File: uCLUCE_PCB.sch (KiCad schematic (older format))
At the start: 19 parts, among them J1 Screw_Terminal_01x03, J2 GS2, P1 USB_A, P2 UART_TTL, U1 PIC16F1455-I/ST, U2 MCP2003B-E/SN, U3 fiducial

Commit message: gerber generation
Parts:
- removed P2: UART_TTL, Pin_Headers:Pin_Header_Straight_1x02_Pitch2.54mm, symbol CONN_01X02
- added P2: UART_TTL, Pin_Headers:Pin_Header_Straight_1x03_Pitch2.54mm, symbol CONN_01X03
- C1, C2, C3: 1st Disrtib Link (none) -> https://www.maritex.com.pl/elementy_pasywne/kondensatory/ko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
- C4, C5: footprint (none) -> Capacitors_SMD:C_0603; 1st Disrtib Link (none) -> https://www.maritex.com.pl/elementy_pasywne/kondensatory/ko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
- R1, R2, R3: 1st Disrtib Link (none) -> https://www.maritex.com.pl/elementy_pasywne/rezystory/rezys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
- U2: footprint Housings_SOIC:SO-8_5.3x6.2mm_Pitch1.27mm -> Housings_SOIC:SOIC-8_3.9x4.9mm_Pitch1.27mm
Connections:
- net GND: now also P2.3 (P3)
- net at R2.1, U1.6 (RC4), U2.1 (Rxd): now also P2.2 (P2)
- net at U1.5 (RC5), U2.4 (TXd): now also P2.1 (P1)
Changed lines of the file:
@@
 F 0 "U2" H 3050 2850 60  0000 C CNN
 F 1 "MCP2003B-E/SN" H 3150 2250 60  0000 C CNN
-F 2 "Housings_SOIC:SO-8_5.3x6.2mm_Pitch1.27mm" H 3000 2350 60  0001 C CNN
+F 2 "Housings_SOIC:SOIC-8_3.9x4.9mm_Pitch1.27mm" H 3000 2350 60  0001 C CNN
 F 3 "" H 3000 2350 60  0001 C CNN
 F 4 "https://octopart.com/mcp2003b-e%2Fsn-microchip-67312985" H 3250 2550 60  0001 C CNN "1st Disrtib Link"
@@
 F 2 "Capacitors_SMD:C_0603" H 6050 2300 50  0001 C CNN
 F 3 "" H 6050 2300 50  0001 C CNN
+F 4 "https://www.maritex.com.pl/elementy_pasywne/kondensatory/kondensatory_ceramiczne/smd_0603/dielektryk_x7r_lub_x5r/cmc0603-470n-kx25-s.html" H 6050 2300 60  0001 C CNN "1st Disrtib Link"
 	1    6050 2300
 	0    1    1    0
 $EndComp
 $Comp
-L GND #PWR16
+L GND #PWR01
 U 1 1 59E21FB8
 P 7350 2150
-F 0 "#PWR16" H 7350 1900 50  0001 C CNN
+F 0 "#PWR01" H 7350 1900 50  0001 C CNN
 F 1 "GND" H 7350 2000 50  0000 C CNN
 F 2 "" H 7350 2150 50  0001 C CNN
@@
 $EndComp
 $Comp
-L +5V #PWR15
+L +5V #PWR02
 U 1 1 59E220C9
 P 6950 2900
-F 0 "#PWR15" H 6950 2750 50  0001 C CNN
+F 0 "#PWR02" H 6950 2750 50  0001 C CNN
 F 1 "+5V" H 6950 3040 50  0000 C CNN
 F 2 "" H 6950 2900 50  0001 C CNN
@@
 $EndComp
 $Comp
-L +5V #PWR11
+L +5V #PWR03
 U 1 1 59E2213F
 P 4050 2000
-F 0 "#PWR11" H 4050 1850 50  0001 C CNN
+F 0 "#PWR03" H 4050 1850 50  0001 C CNN
 F 1 "+5V" H 4050 2140 50  0000 C CNN
 F 2 "" H 4050 2000 50  0001 C CNN
@@
 $EndComp
 $Comp
-L +BATT #PWR1
+L +BATT #PWR04
 U 1 1 59E22154
 P 2000 2200
-F 0 "#PWR1" H 2000 2050 50  0001 C CNN
+F 0 "#PWR04" H 2000 2050 50  0001 C CNN
 F 1 "+BATT" V 1950 2400 50  0000 C CNN
 F 2 "" H 2000 2200 50  0001 C CNN
@@
 $EndComp
 $Comp
-L GND #PWR2
+L GND #PWR05
 U 1 1 59E22180
 P 2400 2200
-F 0 "#PWR2" H 2400 1950 50  0001 C CNN
+F 0 "#PWR05" H 2400 1950 50  0001 C CNN
 F 1 "GND" V 2300 2100 50  0000 C CNN
 F 2 "" H 2400 2200 50  0001 C CNN
@@
 $EndComp
 $Comp
-L GND #PWR14
+L GND #PWR06
 U 1 1 59E230A7
 P 6950 2800
-F 0 "#PWR14" H 6950 2550 50  0001 C CNN
+F 0 "#PWR06" H 6950 2550 50  0001 C CNN
 F 1 "GND" V 6900 2600 50  0001 C CNN
 F 2 "" H 6950 2800 50  0001 C CNN
@@
 MCLR
 $Comp
-L +5V #PWR13
+L +5V #PWR07
 U 1 1 59E237FB
 P 6550 2300
-F 0 "#PWR13" H 6550 2150 50  0001 C CNN
+F 0 "#PWR07" H 6550 2150 50  0001 C CNN
 F 1 "+5V" H 6550 2440 50  0000 C CNN
 F 2 "" H 6550 2300 50  0001 C CNN
@@
 F 2 "Capacitors_SMD:C_0603" H 3450 1850 50  0001 C CNN
 F 3 "" H 3450 1850 50  0001 C CNN
+F 4 "https://www.maritex.com.pl/elementy_pasywne/kondensatory/kondensatory_ceramiczne/smd_0603/dielektryk_x7r_lub_x5r/cmc0603-470n-kx25-s.html" H 3450 1850 60  0001 C CNN "1st Disrtib Link"
 	1    3450 1850
 	-1   0    0    1
 $EndComp
 $Comp
-L +5V #PWR7
+L +5V #PWR08
 U 1 1 59E2335A
 P 3450 1750
-F 0 "#PWR7" H 3450 1600 50  0001 C CNN
+F 0 "#PWR08" H 3450 1600 50  0001 C CNN
 F 1 "+5V" H 3450 1890 50  0000 C CNN
 F 2 "" H 3450 1750 50  0001 C CNN
@@
 $EndComp
 $Comp
-L GND #PWR8
+L GND #PWR09
 U 1 1 59E2337A
 P 3450 1950
-F 0 "#PWR8" H 3450 1700 50  0001 C CNN
+F 0 "#PWR09" H 3450 1700 50  0001 C CNN
 F 1 "GND" H 3450 1800 50  0001 C CNN
 F 2 "" H 3450 1950 50  0001 C CNN
@@
 $EndComp
 $Comp
-L +5V #PWR9
+L +5V #PWR010
 U 1 1 59E233BF
 P 3750 1750
-F 0 "#PWR9" H 3750 1600 50  0001 C CNN
+F 0 "#PWR010" H 3750 1600 50  0001 C CNN
 F 1 "+5V" H 3750 1890 50  0000 C CNN
 F 2 "" H 3750 1750 50  0001 C CNN
@@
 $EndComp
 $Comp
-L GND #PWR10
+L GND #PWR011
 U 1 1 59E23423
 P 3750 1950
-F 0 "#PWR10" H 3750 1700 50  0001 C CNN
+F 0 "#PWR011" H 3750 1700 50  0001 C CNN
 F 1 "GND" H 3750 1800 50  0001 C CNN
 F 2 "" H 3750 1950 50  0001 C CNN
@@
 F 2 "Resistors_SMD:R_0603" H 2650 1450 50  0001 C CNN
 F 3 "" H 2650 1450 50  0001 C CNN
+F 4 "https://www.maritex.com.pl/elementy_pasywne/rezystory/rezystory_smd/rezystory_smd_0603/rezystory_smd_w_rozmiarze_0603_w_tolerancji_5/rmc0603-1k0-s.html" H 2650 1450 60  0001 C CNN "1st Disrtib Link"
 	1    2650 1450
 	1    0    0    -1
 $EndComp
 $Comp
-L +BATT #PWR3
+L +BATT #PWR012
 U 1 1 59E23A89
 P 2650 1050
-F 0 "#PWR3" H 2650 900 50  0001 C CNN
+F 0 "#PWR012" H 2650 900 50  0001 C CNN
 F 1 "+BATT" H 2650 1190 50  0000 C CNN
 F 2 "" H 2650 1050 50  0001 C CNN
@@
 F 2 "Capacitors_SMD:C_0603" H 3750 1850 50  0001 C CNN
 F 3 "" H 3750 1850 50  0001 C CNN
+F 4 "https://www.maritex.com.pl/elementy_pasywne/kondensatory/kondensatory_ceramiczne/smd_0603/dielektryk_x7r_lub_x5r/cmc0603-100n-kx16-s.html" H 3750 1850 60  0001 C CNN "1st Disrtib Link"
 	1    3750 1850
 	-1   0    0    1
@@
 F 2 "Resistors_SMD:R_0603" H 3950 2600 50  0001 C CNN
 F 3 "" H 3950 2600 50  0001 C CNN
+F 4 "https://www.maritex.com.pl/elementy_pasywne/rezystory/rezystory_smd/rezystory_smd_0603/rezystory_smd_0603_w_tolerancji_1/rmc0603-4k7-1-y.html" H 3950 2600 60  0001 C CNN "1st Disrtib Link"
 	1    3950 2600
 	1    0    0    -1
 $EndComp
 $Comp
-L GND #PWR5
+L GND #PWR013
 U 1 1 59E51428
 P 2800 2150
-F 0 "#PWR5" H 2800 1900 50  0001 C CNN
+F 0 "#PWR013" H 2800 1900 50  0001 C CNN
 F 1 "GND" H 2800 2000 50  0001 C CNN
 F 2 "" H 2800 2150 50  0001 C CNN
@@
 $EndComp
 $Comp
-L +5V #PWR12
+L +5V #PWR014
 U 1 1 59E50C40
 P 4150 2950
-F 0 "#PWR12" H 4150 2800 50  0001 C CNN
+F 0 "#PWR014" H 4150 2800 50  0001 C CNN
 F 1 "+5V" H 4150 3090 50  0000 C CNN
 F 2 "" H 4150 2950 50  0001 C CNN
@@
 F 0 "C5" H 2910 2970 50  0000 L CNN
 F 1 "1u" H 2910 2820 50  0000 L CNN
-F 2 "" H 2900 2900 50  0000 C CNN
+F 2 "Capacitors_SMD:C_0603" H 2900 2900 50  0001 C CNN
 F 3 "" H 2900 2900 50  0000 C CNN
+F 4 "https://www.maritex.com.pl/elementy_pasywne/kondensatory/kondensatory_ceramiczne/smd_0603/dielektryk_x7r_lub_x5r/cmc0603-1000n-kx16-s.html" H 2900 2900 60  0001 C CNN "1st Disrtib Link"
 	1    2900 2900
 	1    0    0    -1
@@
 F 0 "C4" H 2810 2120 50  0000 L CNN
 F 1 "220p" H 2810 1970 50  0000 L CNN
-F 2 "" H 2800 2050 50  0000 C CNN
+F 2 "Capacitors_SMD:C_0603" H 2800 2050 50  0001 C CNN
 F 3 "" H 2800 2050 50  0000 C CNN
+F 4 "https://www.maritex.com.pl/elementy_pasywne/kondensatory/kondensatory_ceramiczne/smd_0603/dielektryk_x7r_lub_x5r/cmc0603-680p-kx16-f.html" H 2800 2050 60  0001 C CNN "1st Disrtib Link"
 	1    2800 2050
 	1    0    0    -1
@@
 $EndComp
 $Comp
-L GND #PWR4
+L GND #PWR015
 U 1 1 59E668FA
 P 2700 3000
-F 0 "#PWR4" H 2700 2750 50  0001 C CNN
+F 0 "#PWR015" H 2700 2750 50  0001 C CNN
 F 1 "GND" H 2700 2850 50  0000 C CNN
 F 2 "" H 2700 3000 50  0001 C CNN
@@
 F 2 "Resistors_SMD:R_0603" H 2550 2600 50  0001 C CNN
 F 3 "" H 2550 2600 50  0001 C CNN
+F 4 "https://www.maritex.com.pl/elementy_pasywne/rezystory/rezystory_smd/rezystory_smd_0603/rezystory_smd_w_rozmiarze_0603_w_tolerancji_5/rmc0603-51r-y.html" H 2550 2600 60  0001 C CNN "1st Disrtib Link"
 	1    2550 2600
 	0    1    1    0
@@
 Connection ~ 2700 2800
 $Comp
-L GND #PWR6
+L GND #PWR016
 U 1 1 59E67A70
 P 2900 3000
-F 0 "#PWR6" H 2900 2750 50  0001 C CNN
+F 0 "#PWR016" H 2900 2750 50  0001 C CNN
 F 1 "GND" H 2900 2850 50  0000 C CNN
 F 2 "" H 2900 3000 50  0001 C CNN
@@
 	1900 2600 2050 2600
 Connection ~ 2000 2600
-$Comp
-L CONN_01X02 P2
-U 1 1 59E765D9
-P 3800 3400
-F 0 "P2" H 3800 3550 50  0000 C CNN
-F 1 "UART_TTL" V 3900 3400 50  0000 C CNN
-F 2 "Pin_Headers:Pin_Header_Straight_1x02_Pitch2.54mm" H 3800 3400 50  0001 C CNN
-F 3 "" H 3800 3400 50  0000 C CNN
-	1    3800 3400
-	0    1    1    0
-$EndComp
 Wire Wire Line
 	3750 3200 3750 2700
@@
 	1    0    0    -1
 $EndComp
+$Comp
+L CONN_01X03 P2
+U 1 1 59E7CE46
+P 3750 3400
+F 0 "P2" H 3750 3600 50  0000 C CNN
+F 1 "UART_TTL" V 3850 3400 50  0000 C CNN
+F 2 "Pin_Headers:Pin_Header_Straight_1x03_Pitch2.54mm" H 3750 3400 50  0001 C CNN
+F 3 "" H 3750 3400 50  0000 C CNN
+	1    3750 3400
+	0    1    1    0
+$EndComp
+$Comp
+L GND #PWR?
+U 1 1 59E7D0F4
+P 3650 3200
+F 0 "#PWR?" H 3650 2950 50  0001 C CNN
+F 1 "GND" H 3650 3050 50  0000 C CNN
+F 2 "" H 3650 3200 50  0001 C CNN
+F 3 "" H 3650 3200 50  0001 C CNN
+	1    3650 3200
+	0    1    1    0
+$EndComp
 $EndSCHEMATC

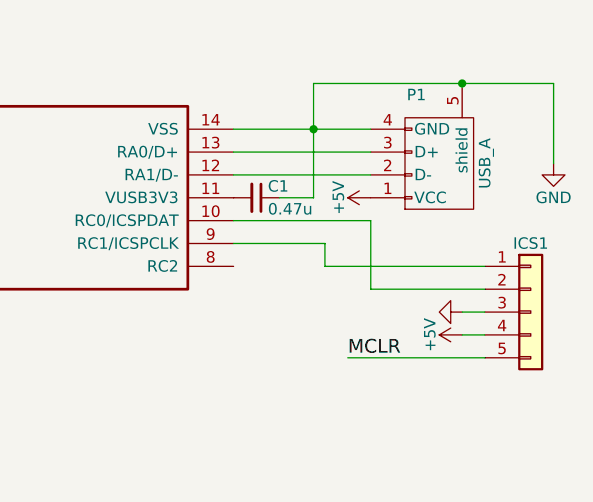
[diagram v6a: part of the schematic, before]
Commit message: Fixed USB Layout
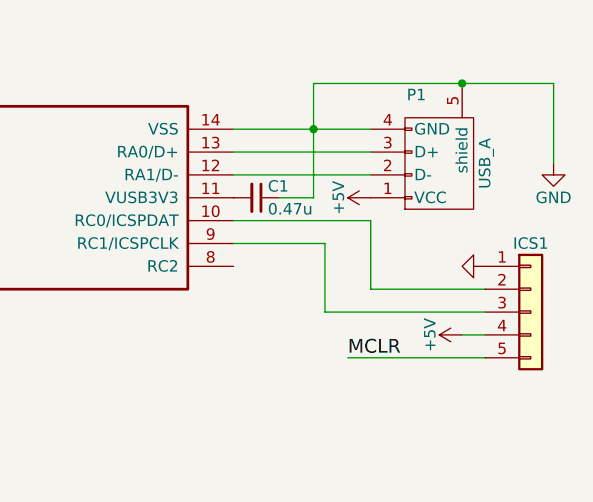
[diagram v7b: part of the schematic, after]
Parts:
- P1: footprint uCLUCE_PCB:USB_A_DS1097 -> uCLUCE_PCB:USB_A_DS1097R
- U3: footprint Fiducials:Fiducial_1mm_Dia_2.54mm_Outer_CopperBottom -> uCLUCE_PCB:FICUCIAL_MIN
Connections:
- net GND: now also ICS1.1 (Pin_1); no longer ICS1.3 (Pin_3)
- net at U1.9 (RC1/ICSPCLK): now also ICS1.3 (Pin_3); no longer ICS1.1 (Pin_1)
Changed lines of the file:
@@
 F 0 "P1" V 7100 2000 50  0000 C CNN
 F 1 "USB_A" H 6800 2300 50  0000 C CNN
-F 2 "uCLUCE_PCB:USB_A_DS1097" V 6800 2000 50  0001 C CNN
+F 2 "uCLUCE_PCB:USB_A_DS1097R" V 6800 2000 50  0001 C CNN
 F 3 "" V 6800 2000 50  0000 C CNN
 F 4 "https://www.maritex.com.pl/zlacza/zlacza_usb_hdmi_ieee/zlacza_i_kable_usb/wtyk_usb_1xa4_katowy/usbp1arw-cv.html" H 6850 2100 60  0001 C CNN "1st Disrtib Link"
@@
 L GND #PWR06
 U 1 1 59E230A7
-P 6950 2800
-F 0 "#PWR06" H 6950 2550 50  0001 C CNN
-F 1 "GND" V 6900 2600 50  0001 C CNN
-F 2 "" H 6950 2800 50  0001 C CNN
-F 3 "" H 6950 2800 50  0001 C CNN
-	1    6950 2800
+P 7050 2600
+F 0 "#PWR06" H 7050 2350 50  0001 C CNN
+F 1 "GND" V 7000 2400 50  0001 C CNN
+F 2 "" H 7050 2600 50  0001 C CNN
+F 3 "" H 7050 2600 50  0001 C CNN
+	1    7050 2600
 	0    1    1    0
 $EndComp
@@
 	7050 2900 6950 2900
 Wire Wire Line
-	7050 2800 6950 2800
-Wire Wire Line
-	6550 2700 7050 2700
-Wire Wire Line
-	6350 2600 7050 2600
-Wire Wire Line
-	6550 2700 6550 2400
-Wire Wire Line
 	6550 2400 5950 2400
 Wire Wire Line
-	6350 2600 6350 2500
+	6350 2500 6350 2800
 Wire Wire Line
 	6350 2500 5950 2500
@@
 F 0 "U3" H 6500 1400 60  0001 C CNN
 F 1 "fiducial" H 6900 1350 60  0000 C CNN
-F 2 "Fiducials:Fiducial_1mm_Dia_2.54mm_Outer_CopperBottom" H 6700 1150 60  0001 C CNN
+F 2 "uCLUCE_PCB:FICUCIAL_MIN" H 6700 1150 60  0001 C CNN
 F 3 "" H 6700 1150 60  0001 C CNN
 	1    6700 1150
@@
 $EndComp
 $Comp
-L GND #PWR?
+L GND #PWR017
 U 1 1 59E7D0F4
 P 3650 3200
-F 0 "#PWR?" H 3650 2950 50  0001 C CNN
+F 0 "#PWR017" H 3650 2950 50  0001 C CNN
 F 1 "GND" H 3650 3050 50  0000 C CNN
 F 2 "" H 3650 3200 50  0001 C CNN
@@
 	0    1    1    0
 $EndComp
+Wire Wire Line
+	6350 2800 7050 2800
+Wire Wire Line
+	6550 2700 6550 2400
+Wire Wire Line
+	6550 2700 7050 2700
 $EndSCHEMATC

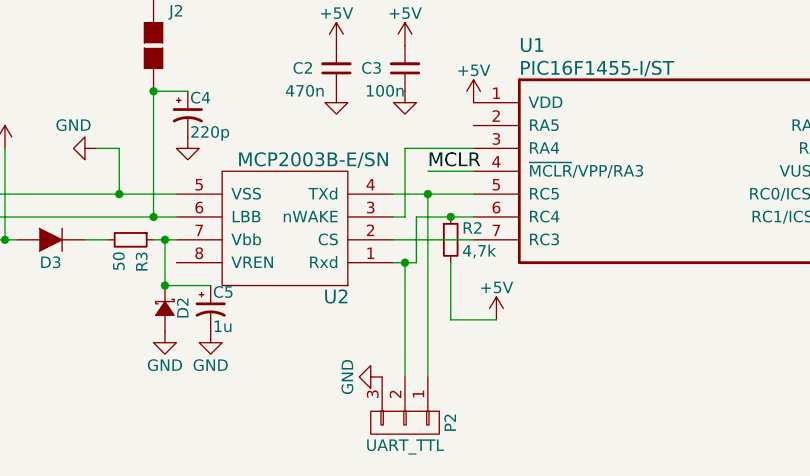
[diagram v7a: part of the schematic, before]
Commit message: Flip LIN RX/TX
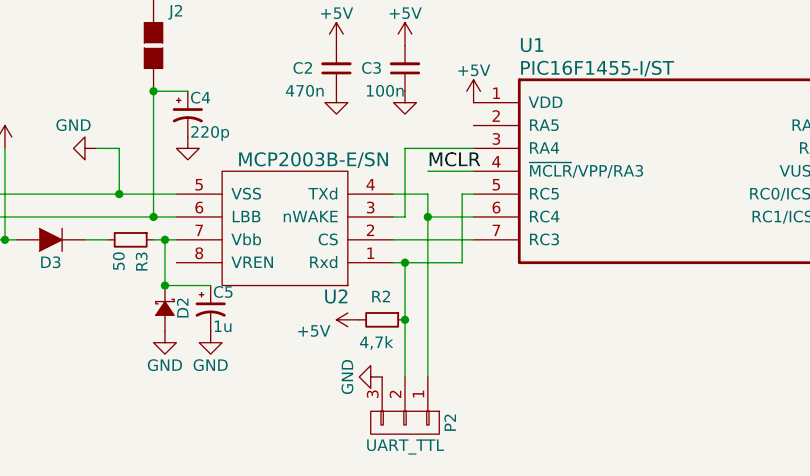
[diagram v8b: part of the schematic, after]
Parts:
- P1: footprint uCLUCE_PCB:USB_A_DS1097R -> uCLUCE_PCB:USB_A_DS1097
- U3: footprint uCLUCE_PCB:FICUCIAL_MIN -> Fiducials:Fiducial_1mm_Dia_2.54mm_Outer_CopperBottom
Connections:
- net at P2.2 (P2), R2.1, U2.1 (Rxd): now also U1.5 (RC5); no longer U1.6 (RC4)
- net at P2.1 (P1), U2.4 (TXd): now also U1.6 (RC4); no longer U1.5 (RC5)
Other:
- moved on the sheet: R2
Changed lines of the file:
@@
 F 0 "P1" V 7100 2000 50  0000 C CNN
 F 1 "USB_A" H 6800 2300 50  0000 C CNN
-F 2 "uCLUCE_PCB:USB_A_DS1097R" V 6800 2000 50  0001 C CNN
+F 2 "uCLUCE_PCB:USB_A_DS1097" V 6800 2000 50  0001 C CNN
 F 3 "" V 6800 2000 50  0000 C CNN
 F 4 "https://www.maritex.com.pl/zlacza/zlacza_usb_hdmi_ieee/zlacza_i_kable_usb/wtyk_usb_1xa4_katowy/usbp1arw-cv.html" H 6850 2100 60  0001 C CNN "1st Disrtib Link"
@@
 L R_Small R2
 U 1 1 59E50B0E
-P 3950 2600
-F 0 "R2" H 4000 2650 50  0000 L CNN
-F 1 "4,7k" H 4000 2550 50  0000 L CNN
-F 2 "Resistors_SMD:R_0603" H 3950 2600 50  0001 C CNN
-F 3 "" H 3950 2600 50  0001 C CNN
-F 4 "https://www.maritex.com.pl/elementy_pasywne/rezystory/rezystory_smd/rezystory_smd_0603/rezystory_smd_0603_w_tolerancji_1/rmc0603-4k7-1-y.html" H 3950 2600 60  0001 C CNN "1st Disrtib Link"
-	1    3950 2600
-	1    0    0    -1
+P 3650 2950
+F 0 "R2" V 3550 2900 50  0000 L CNN
+F 1 "4,7k" V 3750 2850 50  0000 L CNN
+F 2 "Resistors_SMD:R_0603" H 3650 2950 50  0001 C CNN
+F 3 "" H 3650 2950 50  0001 C CNN
+F 4 "https://www.maritex.com.pl/elementy_pasywne/rezystory/rezystory_smd/rezystory_smd_0603/rezystory_smd_0603_w_tolerancji_1/rmc0603-4k7-1-y.html" H 3650 2950 60  0001 C CNN "1st Disrtib Link"
+	1    3650 2950
+	0    1    1    0
 $EndComp
 $Comp
@@
 L +5V #PWR014
 U 1 1 59E50C40
-P 4150 2950
-F 0 "#PWR014" H 4150 2800 50  0001 C CNN
-F 1 "+5V" H 4150 3090 50  0000 C CNN
-F 2 "" H 4150 2950 50  0001 C CNN
-F 3 "" H 4150 2950 50  0001 C CNN
-	1    4150 2950
-	1    0    0    -1
+P 3550 2950
+F 0 "#PWR014" H 3550 2800 50  0001 C CNN
+F 1 "+5V" V 3500 3150 50  0000 C CNN
+F 2 "" H 3550 2950 50  0001 C CNN
+F 3 "" H 3550 2950 50  0001 C CNN
+	1    3550 2950
+	0    -1   -1   0
 $EndComp
 $Comp
@@
 	0    1    1    0
 $EndComp
-Wire Wire Line
-	5950 2100 6550 2100
-Wire Wire Line
-	5950 2200 6550 2200
-Wire Wire Line
-	6300 1800 7350 1800
-Connection ~ 6950 1800
-Wire Wire Line
-	5950 2000 6550 2000
-Wire Wire Line
-	1900 2500 2750 2500
-Wire Wire Line
-	1900 2400 2750 2400
-Connection ~ 2500 2400
-Wire Wire Line
-	7050 2900 6950 2900
-Wire Wire Line
-	6550 2400 5950 2400
-Wire Wire Line
-	6350 2500 6350 2800
-Wire Wire Line
-	6350 2500 5950 2500
-Wire Wire Line
-	6450 3000 7050 3000
-Connection ~ 2650 2500
-Connection ~ 3950 2500
-Wire Wire Line
-	2500 2400 2500 2200
-Wire Wire Line
-	2500 2200 2400 2200
-Wire Wire Line
-	7350 1800 7350 2150
-Wire Wire Line
-	6150 2300 6300 2300
-Wire Wire Line
-	6300 2300 6300 1800
-Connection ~ 6300 2000
-Wire Wire Line
-	3950 2950 3950 2700
-Wire Wire Line
-	4150 2950 3950 2950
-Wire Wire Line
-	4050 2300 3850 2300
-Wire Wire Line
-	3800 2500 4050 2500
-Wire Wire Line
-	3800 2500 3800 2700
-Wire Wire Line
-	4050 2400 3700 2400
-Wire Wire Line
-	3700 2500 3750 2500
-Wire Wire Line
-	3750 2500 3750 2200
-Wire Wire Line
-	3750 2200 4050 2200
-Wire Wire Line
-	3700 2600 4050 2600
-Wire Wire Line
-	3800 2700 3700 2700
-Wire Wire Line
-	2650 2600 2750 2600
-Wire Wire Line
-	2450 2600 2350 2600
-Wire Wire Line
-	2700 2600 2700 2800
-Connection ~ 2700 2600
-Wire Wire Line
-	2700 2800 2900 2800
-Connection ~ 2700 2800
 $Comp
 L GND #PWR016
@@
 	1    0    0    -1
 $EndComp
-Wire Wire Line
-	2650 1950 2650 2500
-Wire Wire Line
-	2800 1950 2650 1950
-Connection ~ 2650 1950
 $Comp
 L D D3
@@
 	-1   0    0    1
 $EndComp
-Wire Wire Line
-	2000 2200 2000 2600
-Wire Wire Line
-	1900 2600 2050 2600
-Connection ~ 2000 2600
-Wire Wire Line
-	3750 3200 3750 2700
-Connection ~ 3750 2700
-Wire Wire Line
-	3850 3200 3850 2400
-Connection ~ 3850 2400
 $Comp
 L fiducial U3
@@
 F 0 "U3" H 6500 1400 60  0001 C CNN
 F 1 "fiducial" H 6900 1350 60  0000 C CNN
-F 2 "uCLUCE_PCB:FICUCIAL_MIN" H 6700 1150 60  0001 C CNN
+F 2 "Fiducials:Fiducial_1mm_Dia_2.54mm_Outer_CopperBottom" H 6700 1150 60  0001 C CNN
 F 3 "" H 6700 1150 60  0001 C CNN
 	1    6700 1150
@@
 $EndComp
 Wire Wire Line
+	5950 2100 6550 2100
+Wire Wire Line
+	5950 2200 6550 2200
+Wire Wire Line
+	6300 1800 7350 1800
+Connection ~ 6950 1800
+Wire Wire Line
+	5950 2000 6550 2000
+Wire Wire Line
+	1900 2500 2750 2500
+Wire Wire Line
+	1900 2400 2750 2400
+Connection ~ 2500 2400
+Wire Wire Line
+	7050 2900 6950 2900
+Wire Wire Line
 	6350 2800 7050 2800
 Wire Wire Line
+	6550 2700 7050 2700
+Wire Wire Line
 	6550 2700 6550 2400
 Wire Wire Line
-	6550 2700 7050 2700
+	6550 2400 5950 2400
+Wire Wire Line
+	6350 2500 6350 2800
+Wire Wire Line
+	6350 2500 5950 2500
+Wire Wire Line
+	6450 3000 7050 3000
+Connection ~ 2650 2500
+Wire Wire Line
+	2500 2400 2500 2200
+Wire Wire Line
+	2500 2200 2400 2200
+Wire Wire Line
+	7350 1800 7350 2150
+Wire Wire Line
+	6150 2300 6300 2300
+Wire Wire Line
+	6300 2300 6300 1800
+Connection ~ 6300 2000
+Wire Wire Line
+	4050 2300 3850 2300
+Wire Wire Line
+	3700 2500 3750 2500
+Wire Wire Line
+	3750 2500 3750 2200
+Wire Wire Line
+	3750 2200 4050 2200
+Wire Wire Line
+	3700 2600 4050 2600
+Wire Wire Line
+	3700 2700 4000 2700
+Wire Wire Line
+	2650 2600 2750 2600
+Wire Wire Line
+	2450 2600 2350 2600
+Wire Wire Line
+	2700 2600 2700 2800
+Connection ~ 2700 2600
+Wire Wire Line
+	2700 2800 2900 2800
+Connection ~ 2700 2800
+Wire Wire Line
+	2650 1950 2650 2500
+Wire Wire Line
+	2800 1950 2650 1950
+Connection ~ 2650 1950
+Wire Wire Line
+	2000 2200 2000 2600
+Wire Wire Line
+	1900 2600 2050 2600
+Connection ~ 2000 2600
+Wire Wire Line
+	3750 3200 3750 2700
+Connection ~ 3750 2700
+Connection ~ 3750 2950
+Wire Wire Line
+	4050 2400 4000 2400
+Wire Wire Line
+	4000 2400 4000 2700
+Wire Wire Line
+	3700 2400 3850 2400
+Wire Wire Line
+	3850 2400 3850 3200
+Wire Wire Line
+	3850 2500 4050 2500
+Connection ~ 3850 2500
 $EndSCHEMATC
